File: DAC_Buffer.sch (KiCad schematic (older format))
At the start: 11 parts, among them U18 AD8021

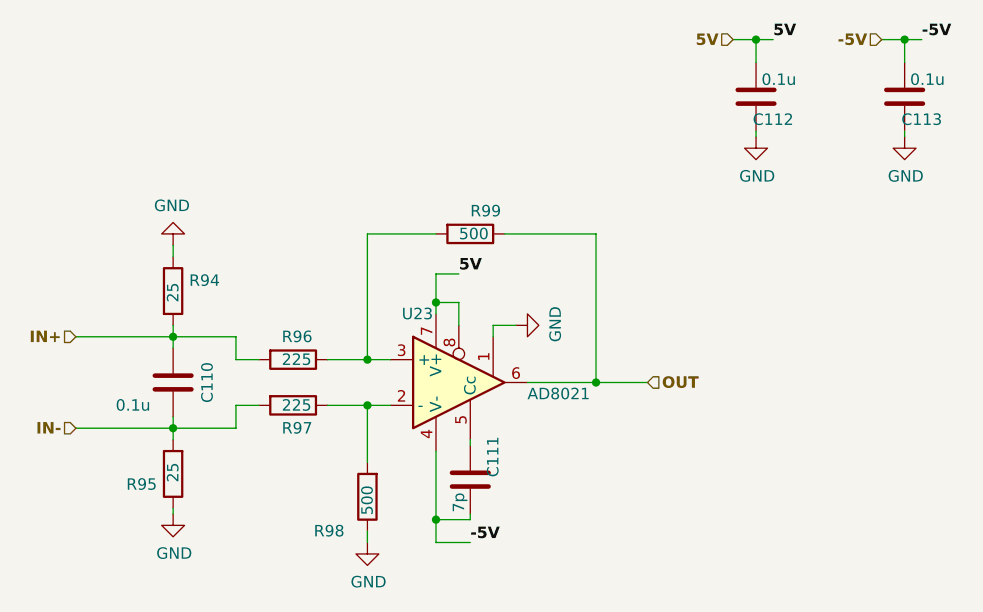
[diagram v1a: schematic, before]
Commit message: Layout done for ADC + LVDS and DAC -> FPGA
Signed-off-by: Alexis Jeandet <alexis.jeandet@member.fsf.org>
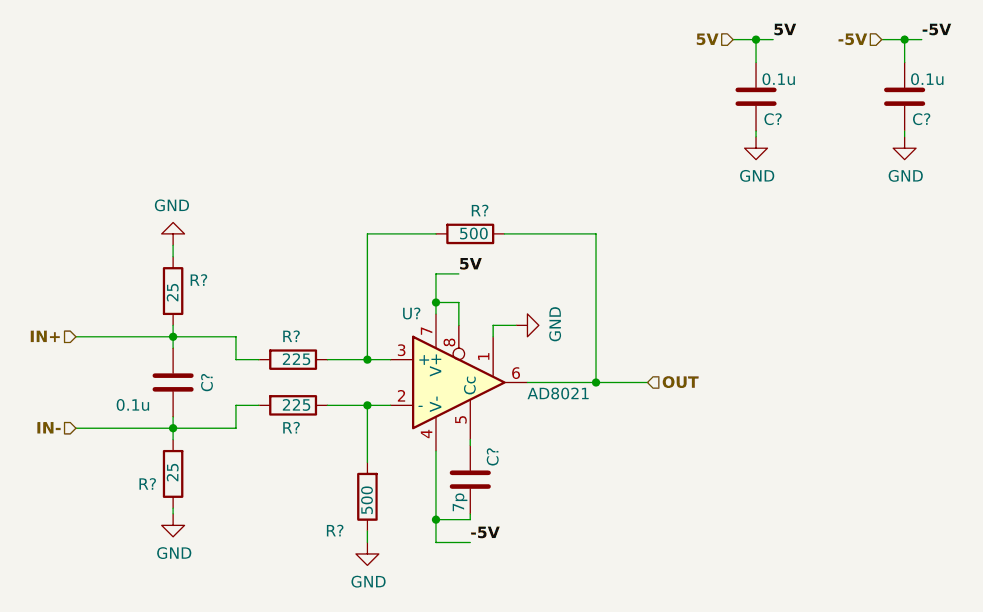
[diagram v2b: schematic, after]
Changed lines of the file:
@@
 AR Path="/5F420A26/5F604603/5F4D5B7A/5F4DCC2C" Ref="#PWR056"  Part="1"
 AR Path="/5F420A26/5F604603/5F53F8D8/5F4DCC2C" Ref="#PWR062"  Part="1"
+AR Path="/5F420A26/5FC968EA/5F4D5B7A/5F4DCC2C" Ref="#PWR?"  Part="1"
+AR Path="/5F420A26/5FC968EA/5F53F8D8/5F4DCC2C" Ref="#PWR?"  Part="1"
 F 0 "#PWR062" H 4250 4225 50  0001 C CNN
 F 1 "GND" H 4255 4302 50  0000 C CNN
@@
 AR Path="/5F420A26/5F604603/5F4D5B7A/5F4DCC38" Ref="#PWR055"  Part="1"
 AR Path="/5F420A26/5F604603/5F53F8D8/5F4DCC38" Ref="#PWR061"  Part="1"
+AR Path="/5F420A26/5FC968EA/5F4D5B7A/5F4DCC38" Ref="#PWR?"  Part="1"
+AR Path="/5F420A26/5FC968EA/5F53F8D8/5F4DCC38" Ref="#PWR?"  Part="1"
 F 0 "#PWR061" H 4250 3050 50  0001 C CNN
 F 1 "GND" H 4255 3127 50  0000 C CNN
@@
 AR Path="/5F420A26/5F604603/5F4D5B7A/5F4DCC44" Ref="#PWR057"  Part="1"
 AR Path="/5F420A26/5F604603/5F53F8D8/5F4DCC44" Ref="#PWR063"  Part="1"
+AR Path="/5F420A26/5FC968EA/5F4D5B7A/5F4DCC44" Ref="#PWR?"  Part="1"
+AR Path="/5F420A26/5FC968EA/5F53F8D8/5F4DCC44" Ref="#PWR?"  Part="1"
 F 0 "#PWR063" H 5100 4350 50  0001 C CNN
 F 1 "GND" H 5105 4427 50  0000 C CNN
@@
 AR Path="/5F420A26/5F604603/5F4D5B7A/5F4DCC4A" Ref="#PWR058"  Part="1"
 AR Path="/5F420A26/5F604603/5F53F8D8/5F4DCC4A" Ref="#PWR064"  Part="1"
+AR Path="/5F420A26/5FC968EA/5F4D5B7A/5F4DCC4A" Ref="#PWR?"  Part="1"
+AR Path="/5F420A26/5FC968EA/5F53F8D8/5F4DCC4A" Ref="#PWR?"  Part="1"
 F 0 "#PWR064" H 5750 3400 50  0001 C CNN
 F 1 "GND" H 5755 3477 50  0000 C CNN
@@
 AR Path="/5F420A26/5F604603/5F4D5B7A/5F4DCC50" Ref="#PWR059"  Part="1"
 AR Path="/5F420A26/5F604603/5F53F8D8/5F4DCC50" Ref="#PWR065"  Part="1"
+AR Path="/5F420A26/5FC968EA/5F4D5B7A/5F4DCC50" Ref="#PWR?"  Part="1"
+AR Path="/5F420A26/5FC968EA/5F53F8D8/5F4DCC50" Ref="#PWR?"  Part="1"
 F 0 "#PWR065" H 6800 2575 50  0001 C CNN
 F 1 "GND" H 6805 2652 50  0000 C CNN
@@
 AR Path="/5F420A26/5F604603/5F4D5B7A/5F4DCC56" Ref="#PWR060"  Part="1"
 AR Path="/5F420A26/5F604603/5F53F8D8/5F4DCC56" Ref="#PWR066"  Part="1"
+AR Path="/5F420A26/5FC968EA/5F4D5B7A/5F4DCC56" Ref="#PWR?"  Part="1"
+AR Path="/5F420A26/5FC968EA/5F53F8D8/5F4DCC56" Ref="#PWR?"  Part="1"
 F 0 "#PWR066" H 7450 2575 50  0001 C CNN
 F 1 "GND" H 7455 2652 50  0000 C CNN
@@
 AR Path="/5F420A26/5F604603/5F4D5B7A/5F4DCC68" Ref="R89"  Part="1"
 AR Path="/5F420A26/5F604603/5F53F8D8/5F4DCC68" Ref="R95"  Part="1"
-F 0 "R95" H 4320 4346 50  0000 L CNN
+AR Path="/5F420A26/5FC968EA/5F4D5B7A/5F4DCC68" Ref="R?"  Part="1"
+AR Path="/5F420A26/5FC968EA/5F53F8D8/5F4DCC68" Ref="R?"  Part="1"
+F 0 "R?" H 4320 4346 50  0000 L CNN
 F 1 "25" V 4250 4250 50  0000 L CNN
 F 2 "Resistor_SMD:R_0603_1608Metric" V 4180 4300 50  0001 C CNN
@@
 AR Path="/5F420A26/5F604603/5F4D5B7A/5F4DCC74" Ref="R88"  Part="1"
 AR Path="/5F420A26/5F604603/5F53F8D8/5F4DCC74" Ref="R94"  Part="1"
-F 0 "R94" H 4320 3546 50  0000 L CNN
+AR Path="/5F420A26/5FC968EA/5F4D5B7A/5F4DCC74" Ref="R?"  Part="1"
+AR Path="/5F420A26/5FC968EA/5F53F8D8/5F4DCC74" Ref="R?"  Part="1"
+F 0 "R?" H 4320 3546 50  0000 L CNN
 F 1 "25" V 4250 3450 50  0000 L CNN
 F 2 "Resistor_SMD:R_0603_1608Metric" V 4180 3500 50  0001 C CNN
@@
 AR Path="/5F420A26/5F604603/5F4D5B7A/5F4DCC7A" Ref="R90"  Part="1"
 AR Path="/5F420A26/5F604603/5F53F8D8/5F4DCC7A" Ref="R96"  Part="1"
-F 0 "R96" V 4675 3750 50  0000 L CNN
+AR Path="/5F420A26/5FC968EA/5F4D5B7A/5F4DCC7A" Ref="R?"  Part="1"
+AR Path="/5F420A26/5FC968EA/5F53F8D8/5F4DCC7A" Ref="R?"  Part="1"
+F 0 "R?" V 4675 3750 50  0000 L CNN
 F 1 "225" V 4775 3750 50  0000 L CNN
 F 2 "Resistor_SMD:R_0603_1608Metric" V 4705 3800 50  0001 C CNN
@@
 AR Path="/5F420A26/5F604603/5F4D5B7A/5F4DCC80" Ref="R91"  Part="1"
 AR Path="/5F420A26/5F604603/5F53F8D8/5F4DCC80" Ref="R97"  Part="1"
-F 0 "R97" V 4875 3950 50  0000 L CNN
+AR Path="/5F420A26/5FC968EA/5F4D5B7A/5F4DCC80" Ref="R?"  Part="1"
+AR Path="/5F420A26/5FC968EA/5F53F8D8/5F4DCC80" Ref="R?"  Part="1"
+F 0 "R?" V 4875 3950 50  0000 L CNN
 F 1 "225" V 4775 3950 50  0000 L CNN
 F 2 "Resistor_SMD:R_0603_1608Metric" V 4705 4000 50  0001 C CNN
@@
 AR Path="/5F420A26/5F604603/5F4D5B7A/5F4DCC86" Ref="R92"  Part="1"
 AR Path="/5F420A26/5F604603/5F53F8D8/5F4DCC86" Ref="R98"  Part="1"
-F 0 "R98" H 5200 4550 50  0000 L CNN
+AR Path="/5F420A26/5FC968EA/5F4D5B7A/5F4DCC86" Ref="R?"  Part="1"
+AR Path="/5F420A26/5FC968EA/5F53F8D8/5F4DCC86" Ref="R?"  Part="1"
+F 0 "R?" H 5200 4550 50  0000 L CNN
 F 1 "500" V 5100 4350 50  0000 L CNN
 F 2 "Resistor_SMD:R_0603_1608Metric" V 5030 4400 50  0001 C CNN
@@
 AR Path="/5F420A26/5F604603/5F4D5B7A/5F4DCC8C" Ref="R93"  Part="1"
 AR Path="/5F420A26/5F604603/5F53F8D8/5F4DCC8C" Ref="R99"  Part="1"
-F 0 "R99" V 5450 3250 50  0000 L CNN
+AR Path="/5F420A26/5FC968EA/5F4D5B7A/5F4DCC8C" Ref="R?"  Part="1"
+AR Path="/5F420A26/5FC968EA/5F53F8D8/5F4DCC8C" Ref="R?"  Part="1"
+F 0 "R?" V 5450 3250 50  0000 L CNN
 F 1 "500" V 5550 3200 50  0000 L CNN
 F 2 "Resistor_SMD:R_0603_1608Metric" V 5480 3250 50  0001 C CNN
@@
 AR Path="/5F420A26/5F604603/5F4D5B7A/5F4DCC98" Ref="C106"  Part="1"
 AR Path="/5F420A26/5F604603/5F53F8D8/5F4DCC98" Ref="C110"  Part="1"
-F 0 "C110" V 4100 3900 50  0000 C CNN
+AR Path="/5F420A26/5FC968EA/5F4D5B7A/5F4DCC98" Ref="C?"  Part="1"
+AR Path="/5F420A26/5FC968EA/5F53F8D8/5F4DCC98" Ref="C?"  Part="1"
+F 0 "C?" V 4100 3900 50  0000 C CNN
 F 1 "0.1u" H 4425 4000 50  0000 C CNN
 F 2 "Capacitor_SMD:C_0603_1608Metric" H 4288 3750 50  0001 C CNN
@@
 AR Path="/5F420A26/5F604603/5F4D5B7A/5F4DCCAA" Ref="C107"  Part="1"
 AR Path="/5F420A26/5F604603/5F53F8D8/5F4DCCAA" Ref="C111"  Part="1"
-F 0 "C111" V 5450 4225 50  0000 C CNN
+AR Path="/5F420A26/5FC968EA/5F4D5B7A/5F4DCCAA" Ref="C?"  Part="1"
+AR Path="/5F420A26/5FC968EA/5F53F8D8/5F4DCCAA" Ref="C?"  Part="1"
+F 0 "C?" V 5450 4225 50  0000 C CNN
 F 1 "7p" V 5600 4425 50  0000 C CNN
 F 2 "Capacitor_SMD:C_0603_1608Metric" H 5588 4175 50  0001 C CNN
@@
 AR Path="/5F420A26/5F604603/5F4D5B7A/5F4DCCB0" Ref="C108"  Part="1"
 AR Path="/5F420A26/5F604603/5F53F8D8/5F4DCCB0" Ref="C112"  Part="1"
-F 0 "C112" H 6725 2750 50  0000 C CNN
+AR Path="/5F420A26/5FC968EA/5F4D5B7A/5F4DCCB0" Ref="C?"  Part="1"
+AR Path="/5F420A26/5FC968EA/5F53F8D8/5F4DCCB0" Ref="C?"  Part="1"
+F 0 "C?" H 6725 2750 50  0000 C CNN
 F 1 "0.1u" H 6700 2575 50  0000 C CNN
 F 2 "Capacitor_SMD:C_0603_1608Metric" H 6838 2500 50  0001 C CNN
@@
 AR Path="/5F420A26/5F604603/5F4D5B7A/5F4DCCB6" Ref="C109"  Part="1"
 AR Path="/5F420A26/5F604603/5F53F8D8/5F4DCCB6" Ref="C113"  Part="1"
-F 0 "C113" H 7525 2550 50  0000 C CNN
+AR Path="/5F420A26/5FC968EA/5F4D5B7A/5F4DCCB6" Ref="C?"  Part="1"
+AR Path="/5F420A26/5FC968EA/5F53F8D8/5F4DCCB6" Ref="C?"  Part="1"
+F 0 "C?" H 7525 2550 50  0000 C CNN
 F 1 "0.1u" H 7550 2725 50  0000 C CNN
 F 2 "Capacitor_SMD:C_0603_1608Metric" H 7488 2500 50  0001 C CNN
@@
 AR Path="/5F420A26/5F604603/5F4D5B7A/5F4DCCBC" Ref="U22"  Part="1"
 AR Path="/5F420A26/5F604603/5F53F8D8/5F4DCCBC" Ref="U23"  Part="1"
-F 0 "U23" H 5250 4200 50  0000 L CNN
+AR Path="/5F420A26/5FC968EA/5F4D5B7A/5F4DCCBC" Ref="U?"  Part="1"
+AR Path="/5F420A26/5FC968EA/5F53F8D8/5F4DCCBC" Ref="U?"  Part="1"
+F 0 "U?" H 5250 4200 50  0000 L CNN
 F 1 "AD8021" H 5800 3850 50  0000 L CNN
 F 2 "AD8021ARZ:SOIC127P600X175-8N" H 5500 3900 50  0001 C CNN

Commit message: Added #3.3V and #1.2V supply, completed ADC to USB board layout, added DAC FPGA to USB board bus.
Signed-off-by: Alexis Jeandet <alexis.jeandet@member.fsf.org>
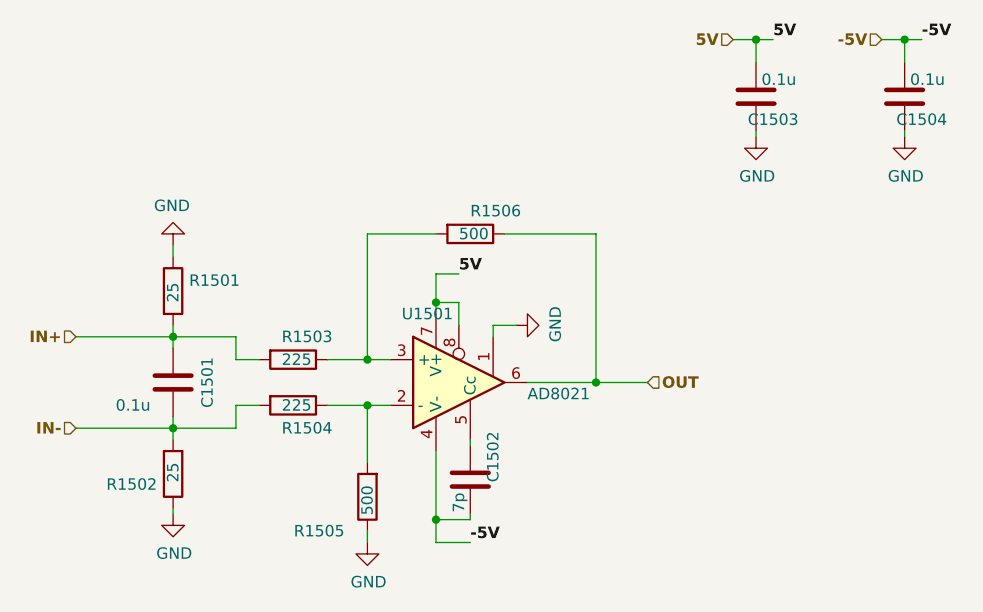
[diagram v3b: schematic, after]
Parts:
- renumbered C81 to C1101, C82 to C1102, C83 to C1103, C84 to C1104, R71 to R1101, R72 to R1102, R73 to R1103, R74 to R1104, R75 to R1105, R76 to R1106, U18 to U1101
